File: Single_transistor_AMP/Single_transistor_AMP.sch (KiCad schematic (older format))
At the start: 10 parts, among them J1 ieeja, J2 Izeja, J3 Barosana, Q1 BC547

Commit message: Majasdarbs peec 8. lekcijas, kur jauzzimee plate
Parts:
- removed J1: ieeja, Connectors:1pin, symbol Conn_01x01
- removed J2: Izeja, Connectors:1pin, symbol Conn_01x01
- removed J3: Barosana, Connectors:AK300-2, symbol Conn_01x02
- added J1: Barosana un ieeja, Connectors:AK300-4, symbol Conn_01x04
- added J2: Izeja, Connectors:AK300-2, symbol Conn_01x02
- added J3: Stiprinajums1, Mounting_Holes:MountingHole_2.2mm_M2_Pad, symbol Conn_01x01
- added J4: Stiprinajums2, Mounting_Holes:MountingHole_2.2mm_M2_Pad, symbol Conn_01x01
- added J5: Stiprinajums3, Mounting_Holes:MountingHole_2.2mm_M2_Pad, symbol Conn_01x01
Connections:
- net +9V: now also J1.4 (Pin_4)
- net GND: now also J1.2 (Pin_2), J1.3 (Pin_3), J2.2 (Pin_2), J3.1 (Pin_1), J4.1 (Pin_1), J5.1 (Pin_1)
- net at Q1.1 (C), R3.2: now also J2.1 (Pin_1)
- net at C1.2: now also J1.1 (Pin_1)
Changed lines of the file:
@@
 LIBS:contrib
 LIBS:valves
+LIBS:Single_transistor_AMP-cache
 EELAYER 25 0
 EELAYER END
@@
 Connection ~ 5600 3200
 Wire Wire Line
-	6000 3900 6000 3600
+	6000 3600 6000 4150
 Wire Wire Line
 	5600 3650 5600 4000
@@
 $EndComp
 Wire Wire Line
-	5100 3900 6000 3900
+	5100 3900 6100 3900
 Wire Wire Line
 	5100 3900 5100 3300
@@
 	5100 2250 5600 2250
 Wire Wire Line
-	5600 2600 6100 2600
+	5600 2600 6200 2600
 Connection ~ 5600 2600
 $Comp
@@
 Connection ~ 5100 2250
 Wire Wire Line
-	4150 2900 4550 2900
+	3800 2900 4550 2900
 $Comp
 L PWR_FLAG #FLG03
@@
 	5500 2250 5500 2200
 Connection ~ 5500 2250
-$Comp
-L Conn_01x01 J2
-U 1 1 5AAA46B5
-P 6300 2600
-F 0 "J2" H 6300 2700 50  0000 C CNN
-F 1 "Izeja" H 6300 2500 50  0000 C CNN
-F 2 "Connectors:1pin" H 6300 2600 50  0001 C CNN
-F 3 "https://eu.mouser.com/ds/2/181/M22-251-1134335.pdf" H 6300 2600 50  0001 C CNN
-	1    6300 2600
-	1    0    0    -1
-$EndComp
-$Comp
-L Conn_01x01 J1
-U 1 1 5AAA4731
-P 3950 2900
-F 0 "J1" H 3950 3000 50  0000 C CNN
-F 1 "ieeja" H 3950 2800 50  0000 C CNN
-F 2 "Connectors:1pin" H 3950 2900 50  0001 C CNN
-F 3 "https://eu.mouser.com/ds/2/181/M22-251-1134335.pdf" H 3950 2900 50  0001 C CNN
-	1    3950 2900
-	-1   0    0    1
-$EndComp
 $Comp
 L PWR_FLAG #FLG04
@@
 Connection ~ 5600 3950
 $Comp
-L Conn_01x02 J3
-U 1 1 5AAA4A96
-P 6750 3150
-F 0 "J3" H 6750 3250 50  0000 C CNN
-F 1 "Barosana" H 6750 2950 50  0000 C CNN
-F 2 "Connectors:AK300-2" H 6750 3150 50  0001 C CNN
-F 3 "http://www.fastelettronica.com/PTR_morsetti.pdf" H 6750 3150 50  0001 C CNN
-	1    6750 3150
-	1    0    0    -1
-$EndComp
-$Comp
-L +9V #PWR05
-U 1 1 5AAA4AF5
-P 6450 3150
-F 0 "#PWR05" H 6450 3000 50  0001 C CNN
-F 1 "+9V" H 6450 3290 50  0000 C CNN
-F 2 "" H 6450 3150 50  0001 C CNN
-F 3 "" H 6450 3150 50  0001 C CNN
-	1    6450 3150
-	1    0    0    -1
-$EndComp
+L Conn_01x02 J2
+U 1 1 5ADF7E08
+P 6400 2600
+F 0 "J2" H 6400 2700 50  0000 C CNN
+F 1 "Izeja" H 6400 2400 50  0000 C CNN
+F 2 "Connectors:AK300-2" H 6400 2600 50  0001 C CNN
+F 3 "https://eu.mouser.com/datasheet/2/16/PCBMETRC-24178.pdf" H 6400 2600 50  0001 C CNN
+	1    6400 2600
+	1    0    0    -1
+$EndComp
+$Comp
+L GND #PWR05
+U 1 1 5ADF7EF4
+P 6150 2750
+F 0 "#PWR05" H 6150 2500 50  0001 C CNN
+F 1 "GND" H 6150 2600 50  0000 C CNN
+F 2 "" H 6150 2750 50  0001 C CNN
+F 3 "" H 6150 2750 50  0001 C CNN
+	1    6150 2750
+	1    0    0    -1
+$EndComp
+Wire Wire Line
+	6200 2700 6150 2700
+Wire Wire Line
+	6150 2700 6150 2750
+$Comp
+L Conn_01x04 J1
+U 1 1 5ADF7F72
+P 3600 2800
+F 0 "J1" H 3600 3000 50  0000 C CNN
+F 1 "Barosana un ieeja" H 3600 2500 50  0000 C CNN
+F 2 "Connectors:AK300-4" H 3600 2800 50  0001 C CNN
+F 3 "https://www.alliedelec.com/m/d/5562820d7d96e18ed6aa6b65b62d0d03.pdf" H 3600 2800 50  0001 C CNN
+	1    3600 2800
+	-1   0    0    1
+$EndComp
+Wire Wire Line
+	3800 2800 4000 2800
+Wire Wire Line
+	4000 2800 4000 2700
+Wire Wire Line
+	4000 2700 3800 2700
 $Comp
 L GND #PWR06
-U 1 1 5AAA4B1D
-P 6450 3250
-F 0 "#PWR06" H 6450 3000 50  0001 C CNN
-F 1 "GND" H 6450 3100 50  0000 C CNN
-F 2 "" H 6450 3250 50  0001 C CNN
-F 3 "" H 6450 3250 50  0001 C CNN
-	1    6450 3250
-	1    0    0    -1
-$EndComp
-Wire Wire Line
-	6550 3150 6450 3150
-Wire Wire Line
-	6550 3250 6450 3250
+U 1 1 5ADF80F6
+P 4100 2750
+F 0 "#PWR06" H 4100 2500 50  0001 C CNN
+F 1 "GND" H 4100 2600 50  0000 C CNN
+F 2 "" H 4100 2750 50  0001 C CNN
+F 3 "" H 4100 2750 50  0001 C CNN
+	1    4100 2750
+	0    -1   -1   0
+$EndComp
+Wire Wire Line
+	4100 2750 4000 2750
+Connection ~ 4000 2750
+$Comp
+L +9V #PWR07
+U 1 1 5ADF8144
+P 4150 2600
+F 0 "#PWR07" H 4150 2450 50  0001 C CNN
+F 1 "+9V" H 4150 2740 50  0000 C CNN
+F 2 "" H 4150 2600 50  0001 C CNN
+F 3 "" H 4150 2600 50  0001 C CNN
+	1    4150 2600
+	1    0    0    -1
+$EndComp
+Wire Wire Line
+	3800 2600 4150 2600
+$Comp
+L Conn_01x01 J3
+U 1 1 5ADF8EFF
+P 6650 3750
+F 0 "J3" H 6650 3850 50  0000 C CNN
+F 1 "Stiprinajums1" H 6650 3650 50  0000 C CNN
+F 2 "Mounting_Holes:MountingHole_2.2mm_M2_Pad" H 6650 3750 50  0001 C CNN
+F 3 "" H 6650 3750 50  0001 C CNN
+	1    6650 3750
+	1    0    0    -1
+$EndComp
+$Comp
+L Conn_01x01 J4
+U 1 1 5ADF8F56
+P 6650 4050
+F 0 "J4" H 6650 4150 50  0000 C CNN
+F 1 "Stiprinajums2" H 6650 3950 50  0000 C CNN
+F 2 "Mounting_Holes:MountingHole_2.2mm_M2_Pad" H 6650 4050 50  0001 C CNN
+F 3 "" H 6650 4050 50  0001 C CNN
+	1    6650 4050
+	1    0    0    -1
+$EndComp
+$Comp
+L Conn_01x01 J5
+U 1 1 5ADF8F8B
+P 6650 4350
+F 0 "J5" H 6650 4450 50  0000 C CNN
+F 1 "Stiprinajums3" H 6650 4250 50  0000 C CNN
+F 2 "Mounting_Holes:MountingHole_2.2mm_M2_Pad" H 6650 4350 50  0001 C CNN
+F 3 "" H 6650 4350 50  0001 C CNN
+	1    6650 4350
+	1    0    0    -1
+$EndComp
+Wire Wire Line
+	6000 3750 6450 3750
+Connection ~ 6000 3750
+Wire Wire Line
+	6100 3900 6100 4050
+Connection ~ 6000 3900
+Wire Wire Line
+	6000 4150 6100 4150
+Wire Wire Line
+	6100 4050 6450 4050
+Wire Wire Line
+	6100 4150 6100 4350
+Wire Wire Line
+	6100 4350 6450 4350
 $EndSCHEMATC

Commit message: Single_transistor_AMP 2. iteraacija
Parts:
- C1: footprint Capacitors_THT:CP_Axial_L10.0mm_D4.5mm_P15.00mm_Horizontal -> Capacitors_THT:C_Rect_L10.0mm_W2.5mm_P7.50mm_MKS4
- C2: footprint Capacitors_THT:CP_Radial_D10.0mm_P2.50mm -> Capacitors_THT:C_Rect_L10.0mm_W2.5mm_P7.50mm_MKS4
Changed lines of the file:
@@
 F 0 "C1" H 4660 2970 50  0000 L CNN
 F 1 "1 uF" H 4660 2820 50  0000 L CNN
-F 2 "Capacitors_THT:CP_Axial_L10.0mm_D4.5mm_P15.00mm_Horizontal" H 4650 2900 50  0001 C CNN
+F 2 "Capacitors_THT:C_Rect_L10.0mm_W2.5mm_P7.50mm_MKS4" H 4650 2900 50  0001 C CNN
 F 3 "https://eu.mouser.com/ds/2/40/spingrd-776981.pdf" H 4650 2900 50  0001 C CNN
 	1    4650 2900
@@
 F 0 "C2" H 6010 3570 50  0000 L CNN
 F 1 "20 uF" H 6010 3420 50  0000 L CNN
-F 2 "Capacitors_THT:CP_Radial_D10.0mm_P2.50mm" H 6000 3500 50  0001 C CNN
+F 2 "Capacitors_THT:C_Rect_L10.0mm_W2.5mm_P7.50mm_MKS4" H 6000 3500 50  0001 C CNN
 F 3 "https://eu.mouser.com/ds/2/281/c49e-506.pdf" H 6000 3500 50  0001 C CNN
 	1    6000 3500

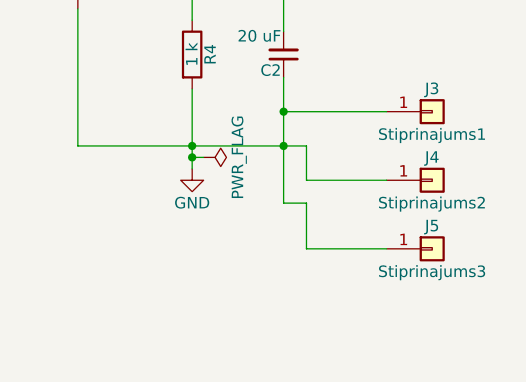
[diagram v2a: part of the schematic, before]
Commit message: Single transistor AMP 2. iteraacija
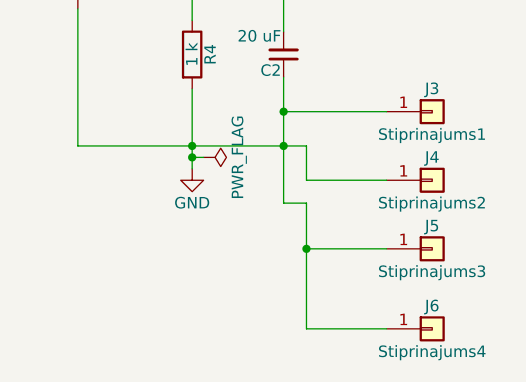
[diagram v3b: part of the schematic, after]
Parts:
- added J6: Stiprinajums4, Mounting_Holes:MountingHole_2.2mm_M2_Pad, symbol Conn_01x01
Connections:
- net GND: now also J6.1 (Pin_1)
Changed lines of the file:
@@
 	6100 4050 6450 4050
 Wire Wire Line
-	6100 4150 6100 4350
+	6100 4150 6100 4700
 Wire Wire Line
 	6100 4350 6450 4350
+$Comp
+L Conn_01x01 J6
+U 1 1 5AE1919A
+P 6650 4700
+F 0 "J6" H 6650 4800 50  0000 C CNN
+F 1 "Stiprinajums4" H 6650 4600 50  0000 C CNN
+F 2 "Mounting_Holes:MountingHole_2.2mm_M2_Pad" H 6650 4700 50  0001 C CNN
+F 3 "" H 6650 4700 50  0001 C CNN
+	1    6650 4700
+	1    0    0    -1
+$EndComp
+Wire Wire Line
+	6100 4700 6450 4700
+Connection ~ 6100 4350
 $EndSCHEMATC
